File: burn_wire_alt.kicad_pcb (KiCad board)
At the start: 2 copper layers, 23 x 24.5 mm, 14 parts, among them J1 TestPoint_THTPad_1.0x1.0mm_Dr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, J2 TestPoint_THTPad_1.0x1.0mm_Dr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, U1 ADP2303ARDZ

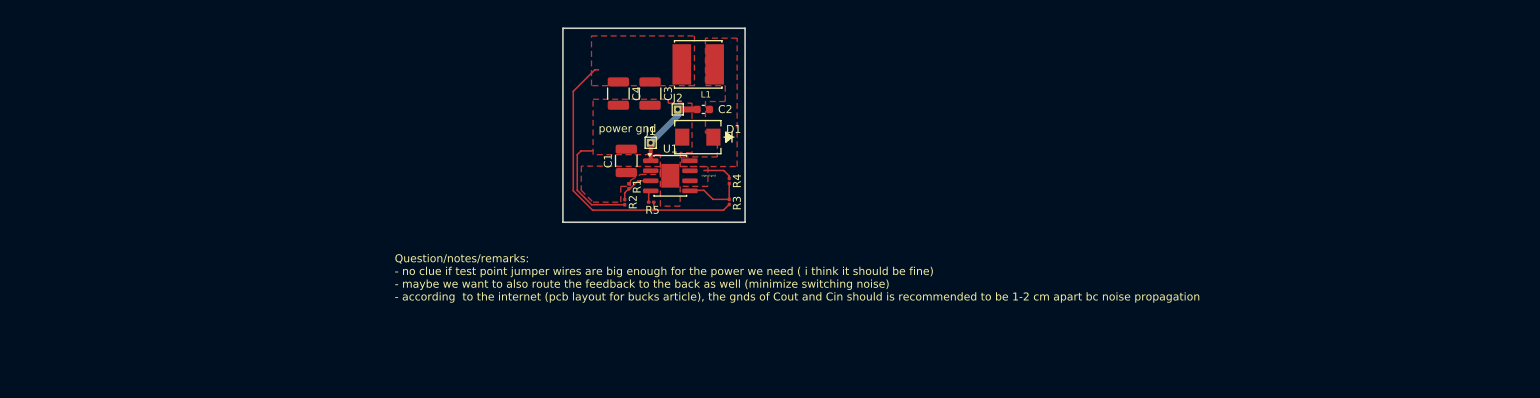
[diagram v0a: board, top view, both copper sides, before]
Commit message: rounded corners
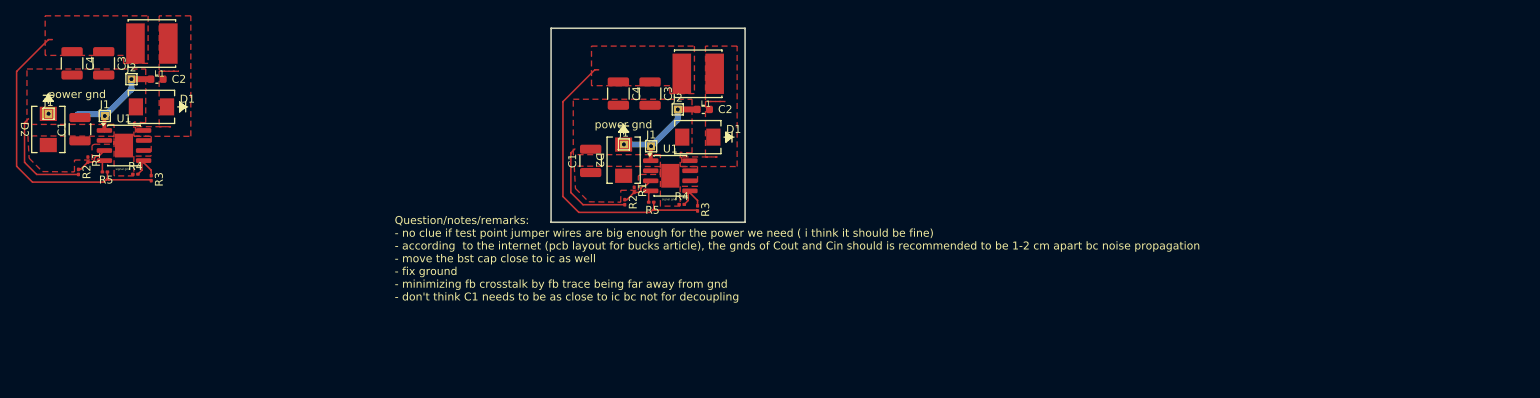
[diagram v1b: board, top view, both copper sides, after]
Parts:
- added C1: 530u, Capacitor_SMD:C_1210_3225Metric, F.Cu at (96.0, 88.5)
- added C2: 0.1u, Capacitor_SMD:C_0603_1608Metric, F.Cu at (105.7, 82.2)
- added C3: 47u, Capacitor_SMD:C_1210_3225Metric, F.Cu at (99.0, 80.2)
- added C4: 47u, Capacitor_SMD:C_1210_3225Metric, F.Cu at (95.0, 80.2)
- added D1: D_Schottky, imported_footprints:CR_SMB_320-345BE_DIO, F.Cu at (105.0, 85.7)
- added D2: D_Schottky, imported_footprints:CR_SMB_320-345BE_DIO-L, F.Cu at (92.0, 88.5)
- added D2: D_Schottky, imported_footprints:CR_SMB_320-345BE_DIO-L, F.Cu at (164.7, 92.4)
- added J1: TestPoint_THTPad_1.0x1.0mm_Drill0.5mm, TestPoint:TestPoint_THTPad_1.0x1.0mm_Drill0.5mm, F.Cu at (92.0, 86.5)
- added J1: TestPoint_THTPad_1.0x1.0mm_Drill0.5mm, TestPoint:TestPoint_THTPad_1.0x1.0mm_Drill0.5mm, F.Cu at (99.1, 86.8)
- added J1: TestPoint_THTPad_1.0x1.0mm_Drill0.5mm, TestPoint:TestPoint_THTPad_1.0x1.0mm_Drill0.5mm, F.Cu at (164.7, 90.4)
- added J2: TestPoint_THTPad_1.0x1.0mm_Drill0.5mm, TestPoint:TestPoint_THTPad_1.0x1.0mm_Drill0.5mm, F.Cu at (102.5, 82.2)
- added L1: 3.3u, imported_footprints:IND_SRN6045TA-3R3Y, F.Cu at (105.1, 77.7)
- added R1: 230k, Resistor_SMD:R_0201_0603Metric, F.Cu at (97.0, 92.3)
- added R2: 100k, Resistor_SMD:R_0201_0603Metric, F.Cu at (95.8, 93.9)
- added R3: 10k, Resistor_SMD:R_0201_0603Metric, F.Cu at (105.0, 94.7)
- added R4: 10k, Resistor_SMD:R_0201_0603Metric, F.Cu at (103.0, 94.2)
- added R5: 100k, Resistor_SMD:R_0201_0603Metric, F.Cu at (99.2, 93.9)
- added U1: ADP2303ARDZ, Package_SO:SOIC-8-1EP_3.9x4.9mm_P1.27mm_EP2.29x3mm, F.Cu at (101.6, 90.6)
- moved R4 6.69 mm to (172.0, 98.0), turned to 180 degrees
- moved C1 4.50 mm to (160.5, 92.5)
- moved R3 4.08 mm to (174.0, 98.5)
- moved L1 1.19 mm to (174.1, 81.5)
- moved R1 0.82 mm to (166.0, 96.2)
- moved J1 0.44 mm to (168.1, 90.7)
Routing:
- net /Vout: track 39.2 -> 74.9 mm
- net /BST: track 10.3 -> 28.4 mm
- net GND: track 17.2 -> 26.3 mm
- net /EN: track 4.77 -> 9.02 mm
- net /PGOOD: track 1.54 -> 3.07 mm
- net /FB: track 7.37 -> 8.61 mm
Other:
- board size 23 x 24.5 mm -> 24.5 x 24.5 mm
- board text added: "Question/notes/remarks: - no clue if test point jumper wires are big enough for the power we need ( i think it should be fine) - according to the internet (pcb layout for bucks article), the gnds of Cout and Cin should is recommended to be 1-2 cm apart bc noise propagation - move the bst cap close to ic as well - fix ground - minimizing fb crosstalk by fb trace being far away from gnd - don't thi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"
- board text removed: "Question/notes/remarks: - no clue if test point jumper wires are big enough for the power we need ( i think it should be fine) - maybe we want to also route the feedback to the back as well (minimize switching noise) - according to the internet (pcb layout for bucks article), the gnds of Cout and Cin should is recommended to be 1-2 cm apart bc noise propagation"

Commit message: cout connected to agnd
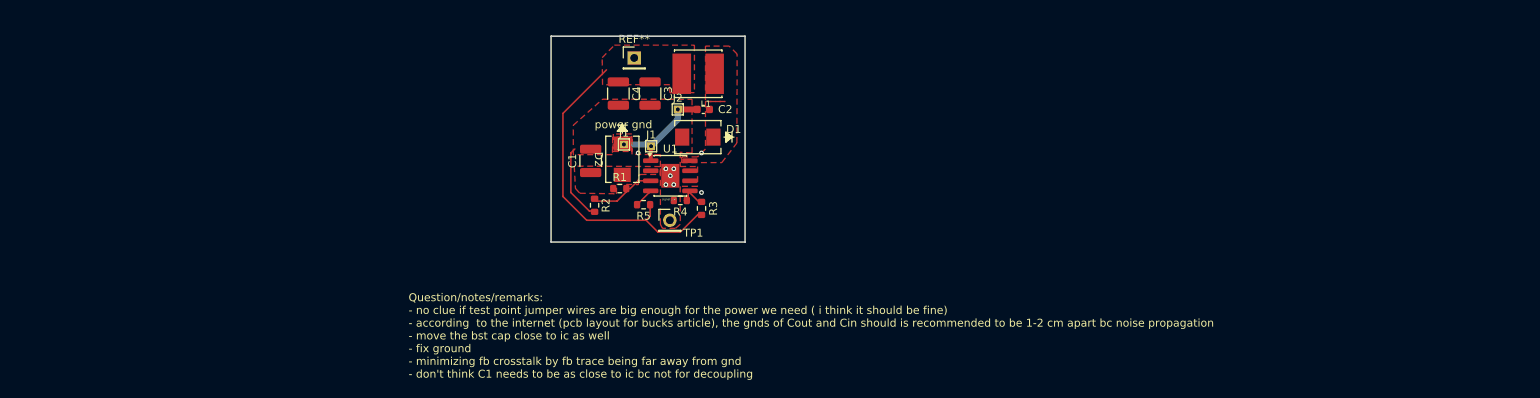
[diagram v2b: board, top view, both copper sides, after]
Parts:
- removed the C1 at (96.0, 88.5)
- removed the C2 at (105.7, 82.2)
- removed the C3 at (99.0, 80.2)
- removed the C4 at (95.0, 80.2)
- removed the D1 at (105.0, 85.7)
- removed the D2 at (92.0, 88.5)
- removed the J1 at (92.0, 86.5)
- removed the J1 at (99.1, 86.8)
- removed the J2 at (102.5, 82.2)
- removed the L1 at (105.1, 77.7)
- removed the R1 at (97.0, 92.3)
- removed the R1 at (166.0, 96.2)
- removed the R2 at (95.8, 93.9)
- removed the R2 at (164.8, 97.7)
- removed the R3 at (105.0, 94.7)
- removed the R3 at (174.0, 98.5)
- removed the R4 at (103.0, 94.2)
- removed the R4 at (172.0, 98.0)
- removed the R5 at (168.2, 97.7)
- removed the R5 at (99.2, 93.9)
- removed the U1 at (101.6, 90.6)
- added R1: 230k, Resistor_SMD:R_0603_1608Metric, F.Cu at (164.2, 96.0)
- added R2: 100k, Resistor_SMD:R_0603_1608Metric, F.Cu at (161.0, 98.1)
- added R3: 10k, Resistor_SMD:R_0603_1608Metric, F.Cu at (174.5, 98.5)
- added R4: 10k, Resistor_SMD:R_0603_1608Metric, F.Cu at (171.8, 97.5)
- added R5: 100k, Resistor_SMD:R_0603_1608Metric, F.Cu at (167.2, 98.0)
- added REF**: PinHeader_1x01_P2.54mm_Vertical, Connector_PinHeader_2.54mm:PinHeader_1x01_P2.54mm_Vertical, F.Cu at (166.0, 79.5)
- added TP1: PinHeader_1x01_P2.54mm_Vertical, Connector_PinHeader_2.54mm:PinHeader_1x01_P2.54mm_Vertical, F.Cu at (170.5, 100.0)
- moved D2 0.20 mm to (164.5, 92.3)
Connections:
- U1 pad 6: GND -> unconnected-(U1-NC-Pad6)
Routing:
- net /Vout: track 74.9 -> 40.7 mm
- net GND: track 26.3 -> 9.92 mm, vias 0 -> 6
- net /BST: track 28.4 -> 14.2 mm
- net /FB: track 8.61 -> 3.70 mm, vias 0 -> 1
- net /EN: track 9.02 -> 8.21 mm
- net /PGOOD: track 3.07 -> 2.46 mm
- net /SW: vias 0 -> 1
- added copper zone on F.Cu, net /BST
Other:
- board size 24.5 x 24.5 mm -> 24.5 x 26 mm
